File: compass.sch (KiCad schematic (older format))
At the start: 14 parts

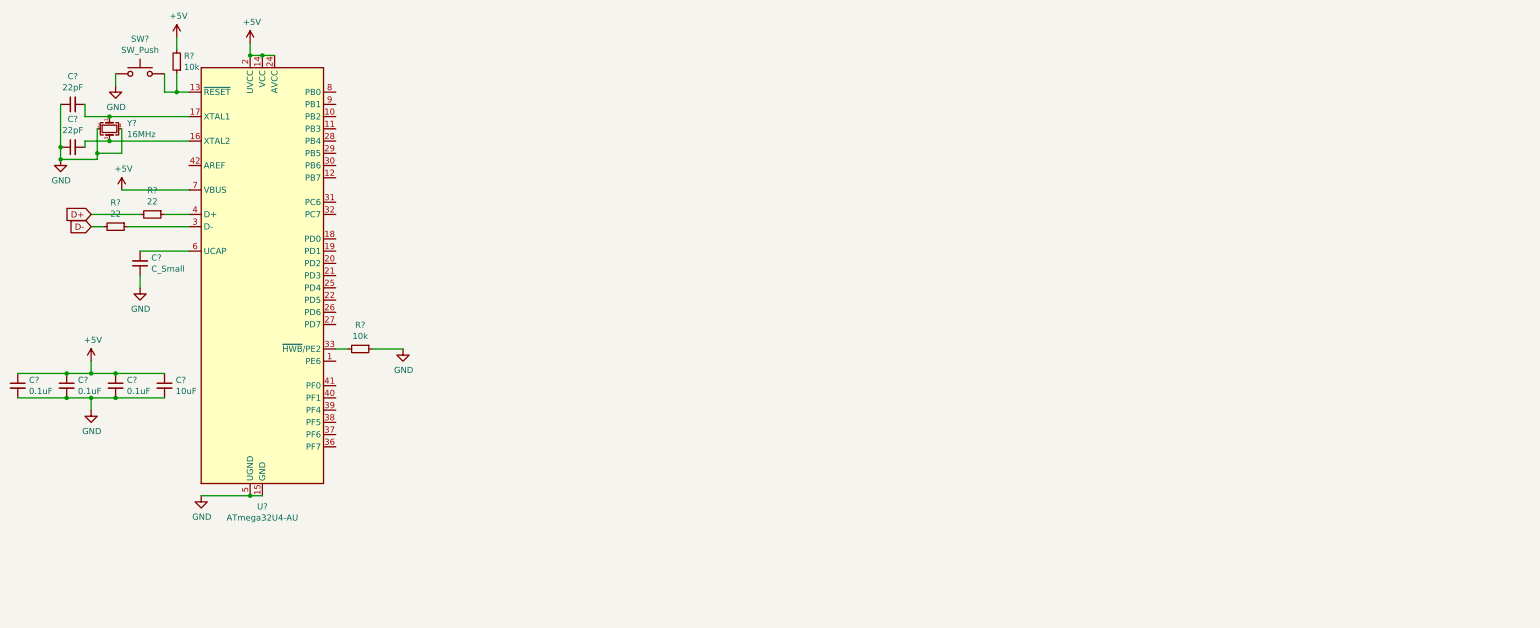
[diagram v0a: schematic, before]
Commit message: added key matrix to schematic
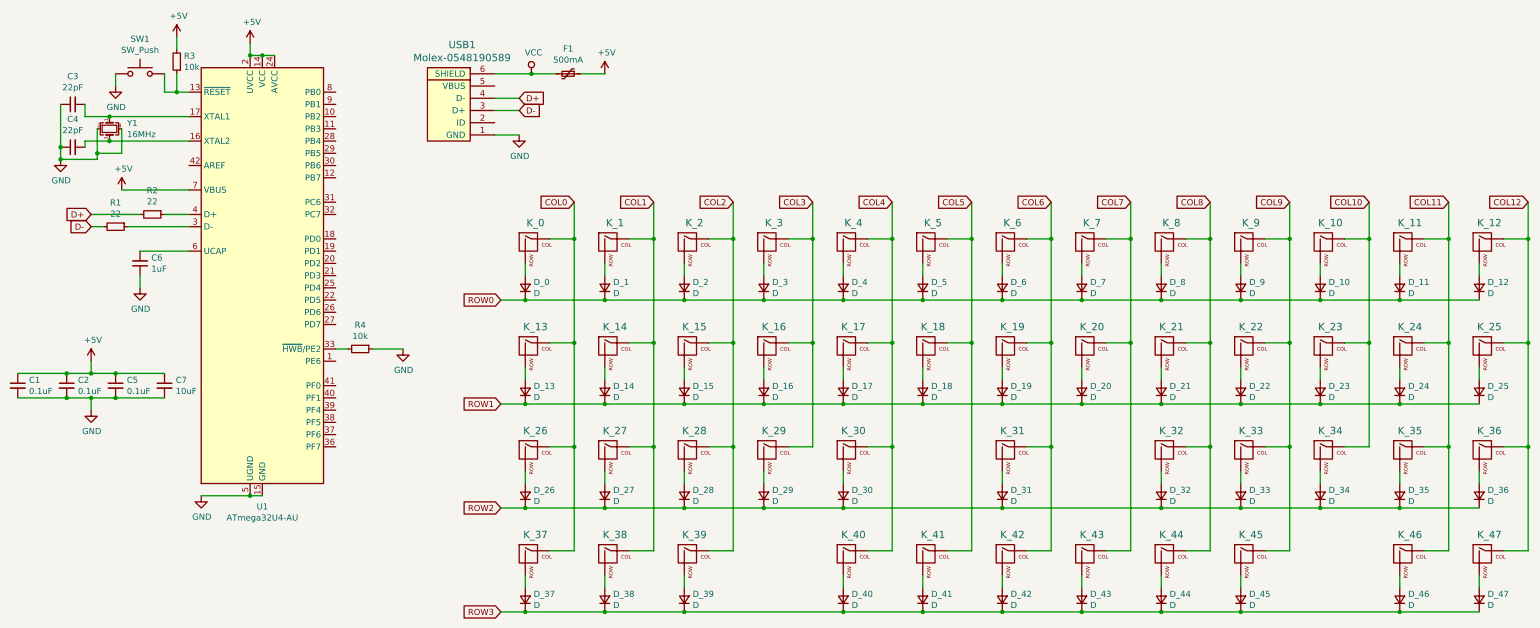
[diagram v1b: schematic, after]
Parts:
- added D_0, D_1, D_10, D_11, D_12, D_13, D_14, D_15, D_16, D_17, D_18, D_19, D_2, D_20, D_21, D_22, D_23, D_24, D_25, D_26, D_27, D_28, D_29, D_3, D_30, D_31, D_32, D_33, D_34, D_35, D_36, D_37, D_38, D_39, D_4, D_40, D_41, D_42, D_43, D_44, D_45, D_46, D_47, D_5, D_6, D_7, D_8, D_9: D, symbol Device:D_Small
- added F1: 500mA, symbol Device:Polyfuse_Small
- added K_0, K_1, K_10, K_11, K_12, K_13, K_14, K_15, K_16, K_17, K_18, K_19, K_2, K_20, K_21, K_22, K_23, K_24, K_25, K_26, K_27, K_28, K_29, K_3, K_30, K_31, K_32, K_33, K_34, K_35, K_36, K_37, K_38, K_39, K_4, K_40, K_41, K_42, K_43, K_44, K_45, K_46, K_47, K_5, K_6, K_7, K_8, K_9: MX-NoLED, symbol MX_Alps_Hybrid:MX-NoLED
- added USB1: Molex-0548190589, symbol random-keyboard-parts:Molex-0548190589
- C6: renamed from C?; value C_Small -> 1uF
- gave numbers to parts that had none: 13
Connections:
- net +5V: now also F1.1
- net D+: now also USB1.4 (D-)
- net D-: now also USB1.3 (D+)
- net GND: now also USB1.1 (GND)
- new net: D_0.2 (A), K_0.2 (ROW)
- new net: D_1.2 (A), K_1.2 (ROW)
- new net: D_2.2 (A), K_2.2 (ROW)
- new net: D_3.2 (A), K_3.2 (ROW)
- new net: D_4.2 (A), K_4.2 (ROW)
- new net: D_5.2 (A), K_5.2 (ROW)
- new net: D_6.2 (A), K_6.2 (ROW)
- new net: D_13.2 (A), K_13.2 (ROW)
- new net: D_14.2 (A), K_14.2 (ROW)
- new net: D_15.2 (A), K_15.2 (ROW)
- new net: D_16.2 (A), K_16.2 (ROW)
- new net: D_17.2 (A), K_17.2 (ROW)
- new net: D_18.2 (A), K_18.2 (ROW)
- new net: D_7.2 (A), K_7.2 (ROW)
- new net: D_8.2 (A), K_8.2 (ROW)
- new net: D_9.2 (A), K_9.2 (ROW)
- new net: D_10.2 (A), K_10.2 (ROW)
- new net: D_11.2 (A), K_11.2 (ROW)
- new net: D_12.2 (A), K_12.2 (ROW)
- new net: D_24.2 (A), K_24.2 (ROW)
- new net: D_23.2 (A), K_23.2 (ROW)
- new net: D_22.2 (A), K_22.2 (ROW)
- new net: D_21.2 (A), K_21.2 (ROW)
- new net: D_20.2 (A), K_20.2 (ROW)
- new net: D_19.2 (A), K_19.2 (ROW)
- new net: D_25.2 (A), K_25.2 (ROW)
- new net: D_30.2 (A), K_30.2 (ROW)
- new net: D_29.2 (A), K_29.2 (ROW)
- new net: D_28.2 (A), K_28.2 (ROW)
- new net: D_27.2 (A), K_27.2 (ROW)
- new net: D_26.2 (A), K_26.2 (ROW)
- new net: D_35.2 (A), K_35.2 (ROW)
- new net: D_34.2 (A), K_34.2 (ROW)
- new net: D_33.2 (A), K_33.2 (ROW)
- new net: D_32.2 (A), K_32.2 (ROW)
- new net: D_31.2 (A), K_31.2 (ROW)
- new net: D_36.2 (A), K_36.2 (ROW)
- new net: D_41.2 (A), K_41.2 (ROW)
- new net: D_40.2 (A), K_40.2 (ROW)
- new net: D_39.2 (A), K_39.2 (ROW)
- new net: D_38.2 (A), K_38.2 (ROW)
- new net: D_37.2 (A), K_37.2 (ROW)
- new net: D_46.2 (A), K_46.2 (ROW)
- new net: D_45.2 (A), K_45.2 (ROW)
- new net: D_44.2 (A), K_44.2 (ROW)
- new net: D_43.2 (A), K_43.2 (ROW)
- new net: D_42.2 (A), K_42.2 (ROW)
- new net: D_47.2 (A), K_47.2 (ROW)
- new net COL0: K_0.1 (COL), K_13.1 (COL), K_26.1 (COL), K_37.1 (COL)
- new net COL1: K_1.1 (COL), K_14.1 (COL), K_27.1 (COL), K_38.1 (COL)
- new net COL10: K_10.1 (COL), K_23.1 (COL), K_34.1 (COL)
- new net COL11: K_11.1 (COL), K_24.1 (COL), K_35.1 (COL), K_46.1 (COL)
- new net COL12: K_12.1 (COL), K_25.1 (COL), K_36.1 (COL), K_47.1 (COL)
- new net COL2: K_15.1 (COL), K_2.1 (COL), K_28.1 (COL), K_39.1 (COL)
- new net COL3: K_16.1 (COL), K_29.1 (COL), K_3.1 (COL)
- new net COL4: K_17.1 (COL), K_30.1 (COL), K_4.1 (COL), K_40.1 (COL)
- new net COL5: K_18.1 (COL), K_41.1 (COL), K_5.1 (COL)
- new net COL6: K_19.1 (COL), K_31.1 (COL), K_42.1 (COL), K_6.1 (COL)
- new net COL7: K_20.1 (COL), K_43.1 (COL), K_7.1 (COL)
- new net COL8: K_21.1 (COL), K_32.1 (COL), K_44.1 (COL), K_8.1 (COL)
- new net COL9: K_22.1 (COL), K_33.1 (COL), K_45.1 (COL), K_9.1 (COL)
- new net ROW0: D_0.1 (K), D_1.1 (K), D_10.1 (K), D_11.1 (K), D_12.1 (K), D_2.1 (K), D_3.1 (K), D_4.1 (K), D_5.1 (K), D_6.1 (K), D_7.1 (K), D_8.1 (K), D_9.1 (K)
- new net ROW1: D_13.1 (K), D_14.1 (K), D_15.1 (K), D_16.1 (K), D_17.1 (K), D_18.1 (K), D_19.1 (K), D_20.1 (K), D_21.1 (K), D_22.1 (K), D_23.1 (K), D_24.1 (K), D_25.1 (K)
- new net ROW2: D_26.1 (K), D_27.1 (K), D_28.1 (K), D_29.1 (K), D_30.1 (K), D_31.1 (K), D_32.1 (K), D_33.1 (K), D_34.1 (K), D_35.1 (K), D_36.1 (K)
- new net ROW3: D_37.1 (K), D_38.1 (K), D_39.1 (K), D_40.1 (K), D_41.1 (K), D_42.1 (K), D_43.1 (K), D_44.1 (K), D_45.1 (K), D_46.1 (K), D_47.1 (K)
- new net VCC: F1.2, USB1.6 (SHIELD)

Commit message: assigned key footprints
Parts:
- K_0, K_1, K_10, K_11, K_12, K_13, K_14, K_15, K_16, K_17, K_18, K_19, K_2, K_20, K_21, K_22, K_23, K_24, K_25, K_26, K_27, K_28, K_29, K_3, K_30, K_31, K_32, K_33, K_34, K_35, K_36, K_37, K_38, K_39, K_4, K_41, K_42, K_43, K_45, K_46, K_47, K_5, K_6, K_7, K_8, K_9: footprint (none) -> MX_Alps_Hybrid:MX-1U-NoLED
- K_40, K_44: footprint (none) -> MX_Alps_Hybrid:MX-1.75U-NoLED
- SW1: footprint (none) -> random-keyboard-parts:SKQG-1155865
- USB1: footprint (none) -> random-keyboard-parts:Molex-0548190589

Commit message: assigned footprints all components
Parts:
- C1, C2, C3, C4, C5, C6, C7: footprint (none) -> Capacitor_SMD:C_0805_2012Metric
- D_0, D_1, D_10, D_11, D_12, D_13, D_14, D_15, D_16, D_17, D_18, D_19, D_2, D_20, D_21, D_22, D_23, D_24, D_25, D_26, D_27, D_28, D_29, D_3, D_30, D_31, D_32, D_33, D_34, D_35, D_36, D_37, D_38, D_39, D_4, D_40, D_41, D_42, D_43, D_44, D_45, D_46, D_47, D_5, D_6, D_7, D_8, D_9: footprint (none) -> Diode_SMD:D_SOD-123
- F1: footprint (none) -> Fuse:Fuse_1206_3216Metric
- R1, R2, R3, R4: footprint (none) -> Resistor_SMD:R_0805_2012Metric
- Y1: footprint (none) -> Crystal:Crystal_SMD_3225-4Pin_3.2x2.5mm
